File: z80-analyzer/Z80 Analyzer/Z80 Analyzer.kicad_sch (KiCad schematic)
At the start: 48 parts, among them J1 Conn_01x40_Pin, M1 TestPoint, U1 Z80CPU

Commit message: [Z80] Layout update
Mostly done, missing:
* Size
* Aligned slots for socket stack securing
* Grounding lead pads
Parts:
- added RN9: R_Pack04_SIP_Split, Resistor_SMD:R_Array_Convex_4x0603, symbol Device:R_Pack04_Split
- RN1, RN3, RN4, RN5, RN7, RN8: symbol Device:R_Pack04_SIP_Split -> Device:R_Pack04_Split
- RN2, RN6: value R_Pack04_SIP_Split -> R_Pack04_Split; symbol Device:R_Pack04_SIP_Split -> Device:R_Pack04_Split
- renumbered TP_RESET1 to RESET1
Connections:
- net at J1.29 (Pin_29): now also RN3.5 (R4.2); no longer RN3.8 (R4.2)
- net at J1.8 (Pin_8): now also RN5.8 (R1.2); no longer RN5.2 (R1.2)
- net at RN7.6 (R3.2): now also J1.28 (Pin_28)
- net at J1.31 (Pin_31): now also RN4.8 (R1.2); no longer RN4.2 (R1.2)
- net at J1.17 (Pin_17): now also RN1.7 (R2.2); no longer RN1.4 (R2.2)
- net at J1.16 (Pin_16): now also RN6.8 (R1.2); no longer RN6.2 (R1.2)
- net at J1.21 (Pin_21): now also RN1.5 (R4.2); no longer RN1.8 (R4.2)
- net at J1.14 (Pin_14): now also RN5.5 (R4.2); no longer RN5.8 (R4.2)
- net at RN8.6 (R3.2): now also J1.36 (Pin_36)
- net at J1.15 (Pin_15): now also RN1.8 (R1.2); no longer RN1.2 (R1.2)
- net at J1.23 (Pin_23): now also RN3.8 (R1.2); no longer RN3.2 (R1.2)
- net at J1.37 (Pin_37): now also RN4.5 (R4.2); no longer RN4.8 (R4.2)
- net at J1.7 (Pin_7): now also RN2.8 (R1.2); no longer RN2.2 (R1.2)
- net at J1.9 (Pin_9): now also RN2.7 (R2.2); no longer RN2.4 (R2.2)
- net at J1.25 (Pin_25): now also RN3.7 (R2.2); no longer RN3.4 (R2.2)
- net at J1.18 (Pin_18): now also RN6.7 (R2.2); no longer RN6.4 (R2.2)
- net at J1.10 (Pin_10): now also RN5.7 (R2.2); no longer RN5.4 (R2.2)
- net at J1.13 (Pin_13): now also RN2.5 (R4.2); no longer RN2.8 (R4.2)
- net at J1.22 (Pin_22): now also RN6.5 (R4.2); no longer RN6.8 (R4.2)
- net at J1.24 (Pin_24): now also RN7.8 (R1.2)
- net at J1.26 (Pin_26): now also RN7.7 (R2.2)
- net at J1.3 (Pin_3): now also RN9.6 (R3.2)
- net at J1.30 (Pin_30): now also RN7.5 (R4.2)
- net at J1.32 (Pin_32): now also RN8.8 (R1.2)
- net at J1.33 (Pin_33): now also RN4.7 (R2.2); no longer RN4.4 (R2.2)
- net at J1.34 (Pin_34): now also RN8.7 (R2.2)
- net at J1.38 (Pin_38): now also RN8.5 (R4.2)
- net at J1.4 (Pin_4): now also RN9.5 (R4.2)
- net A0 renamed S_A0
- net A1 renamed S_A1
- net S_A1: now also RN2.2 (R2.1); no longer RN2.3 (R2.1)
- net A10 renamed S_A10
- net S_A10: now also RN3.3 (R3.1); no longer RN3.5 (R3.1)
- net A11 renamed S_A11
- net S_A11: now also RN3.4 (R4.1); no longer RN3.7 (R4.1)
- net A12 renamed S_A12
- net A13 renamed S_A13
- net S_A13: now also RN4.2 (R2.1); no longer RN4.3 (R2.1)
- net A14 renamed S_A14
- net S_A14: now also RN4.3 (R3.1); no longer RN4.5 (R3.1)
- net A15 renamed S_A15
- net S_A15: now also RN4.4 (R4.1); no longer RN4.7 (R4.1)
- net A2 renamed S_A2
- net S_A2: now also RN2.3 (R3.1); no longer RN2.5 (R3.1)
- net A3 renamed S_A3
- net S_A3: now also RN2.4 (R4.1); no longer RN2.7 (R4.1)
- net A4 renamed S_A4
- net A5 renamed S_A5
- net S_A5: now also RN1.2 (R2.1); no longer RN1.3 (R2.1)
- net A6 renamed S_A6
- net S_A6: now also RN1.3 (R3.1); no longer RN1.5 (R3.1)
- net A7 renamed S_A7
- net S_A7: now also RN1.4 (R4.1); no longer RN1.7 (R4.1)
- net A8 renamed S_A8
- net A9 renamed S_A9
- net S_A9: now also RN3.2 (R2.1); no longer RN3.3 (R2.1)
- net BUSACK renamed S_BUSACK
- net BUSRQ renamed S_BUSRQ
- net CLK renamed S_CLK
- net S_CLK: now also RN9.3 (R3.1), RN9.4 (R4.1); no longer RN8.1 (R1.1)
- net D0 renamed S_D0
- net D1 renamed S_D1
- net S_D1: now also RN5.2 (R2.1); no longer RN5.3 (R2.1)
- net D2 renamed S_D2
- net S_D2: now also RN5.3 (R3.1); no longer RN5.5 (R3.1)
- net D3 renamed S_D3
- net S_D3: now also RN5.4 (R4.1); no longer RN5.7 (R4.1)
- net D4 renamed S_D4
- net D5 renamed S_D5
- net S_D5: now also RN6.2 (R2.1); no longer RN6.3 (R2.1)
- net D6 renamed S_D6
- net S_D6: now also RN6.3 (R3.1); no longer RN6.5 (R3.1)
- net D7 renamed S_D7
- net S_D7: now also RN6.4 (R4.1); no longer RN6.7 (R4.1)
- net HALT renamed S_HALT
- net INT renamed S_INT
- net S_INT: now also RN8.3 (R3.1); no longer RN8.5 (R3.1)
- net IORQ renamed S_IORQ
- net S_IORQ: now also RN7.3 (R3.1); no longer RN7.5 (R3.1)
- net M1 renamed S_M1
- net S_M1: now also RN8.2 (R2.1); no longer RN8.3 (R2.1)
- net MREQ renamed S_MREQ
- net S_MREQ: now also RN7.4 (R4.1); no longer RN7.7 (R4.1)
- net NMI renamed S_NMI
- net S_NMI: now also RN8.4 (R4.1); no longer RN8.7 (R4.1)
- net RD renamed S_RD
- net S_RD: now also RN7.2 (R2.1); no longer RN7.3 (R2.1)
- net RESET renamed S_RESET
- net S_RESET: now also RN8.1 (R1.1)
- net RFSH renamed S_RFSH
- net WAIT renamed S_WAIT
- net WR renamed S_WR
- no-connect marks 0 -> 2
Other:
- note added: "The following signals are not on the Logic Analyzer connector: BUSRQ BUSAQ HALT WAIT RFSH CLK is used for triggering"
- note removed: "The following signals are not on the Logic Analyzer connector: BUSRQ BUSAQ HALT WAIT RFSH RESET"

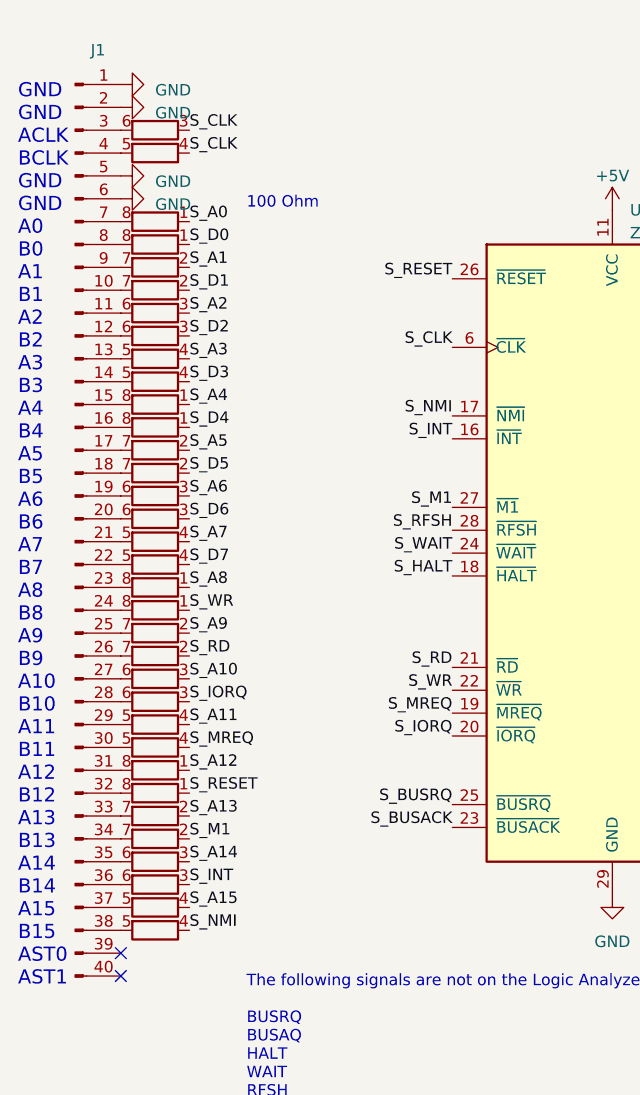
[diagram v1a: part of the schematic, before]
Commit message: [Z80] New routing, just needs rechecking now
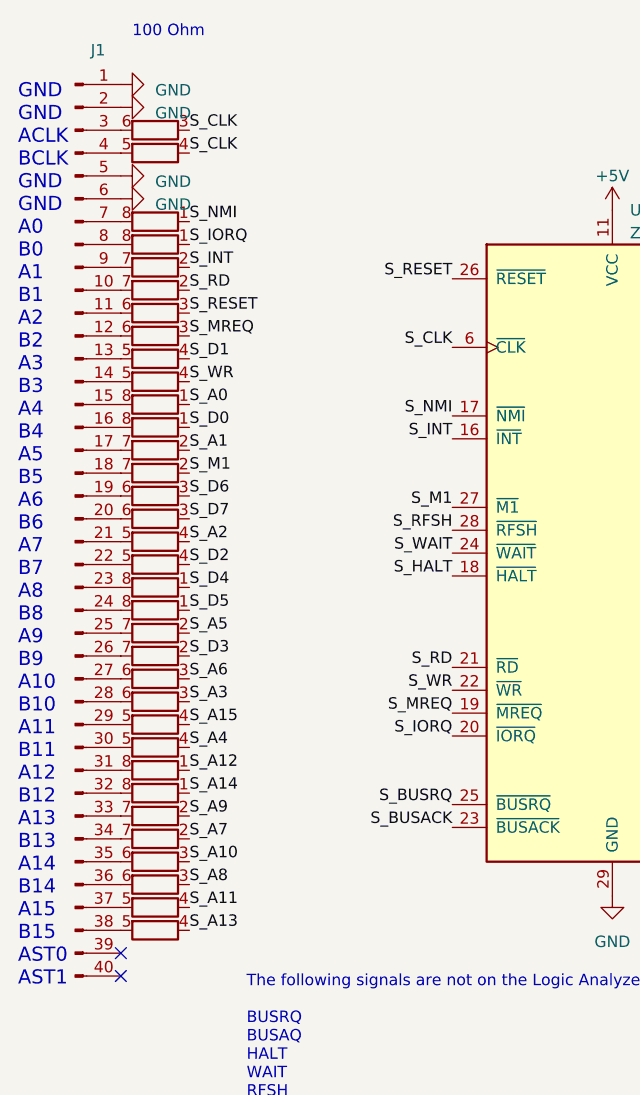
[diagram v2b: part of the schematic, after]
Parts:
- A0, A1, A10, A11, A12, A13, A14, A15, A2, A3, A4, A5, A6, A7, A8, A9, BUSACK1, BUSRQ1, CLK1, D0, D1, D2, D3, D4, D5, D6, D7, HALT1, INT1, IORQ1, M1, MREQ1, NMI1, RD1, RESET1, RFSH1, WAIT1, WR1: footprint TestPoint:TestPoint_Loop_D1.80mm_Drill1.0mm_Beaded -> CustomFootprints:TestPoint_Keystone_5021
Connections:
- net S_A0: now also RN1.1 (R1.1); no longer RN2.1 (R1.1)
- net S_A1: now also RN1.2 (R2.1); no longer RN2.2 (R2.1)
- net S_A10: now also RN4.3 (R3.1); no longer RN3.3 (R3.1)
- net S_A11: now also RN4.4 (R4.1); no longer RN3.4 (R4.1)
- net S_A13: now also RN8.4 (R4.1); no longer RN4.2 (R2.1)
- net S_A14: now also RN8.1 (R1.1); no longer RN4.3 (R3.1)
- net S_A15: now also RN3.4 (R4.1); no longer RN4.4 (R4.1)
- net S_A2: now also RN1.4 (R4.1); no longer RN2.3 (R3.1)
- net S_A3: now also RN7.3 (R3.1); no longer RN2.4 (R4.1)
- net S_A4: now also RN7.4 (R4.1); no longer RN1.1 (R1.1)
- net S_A5: now also RN3.2 (R2.1); no longer RN1.2 (R2.1)
- net S_A6: now also RN3.3 (R3.1); no longer RN1.3 (R3.1)
- net S_A7: now also RN8.2 (R2.1); no longer RN1.4 (R4.1)
- net S_A8: now also RN8.3 (R3.1); no longer RN3.1 (R1.1)
- net S_A9: now also RN4.2 (R2.1); no longer RN3.2 (R2.1)
- net S_D0: now also RN6.1 (R1.1); no longer RN5.1 (R1.1)
- net S_D1: now also RN2.4 (R4.1); no longer RN5.2 (R2.1)
- net S_D2: now also RN6.4 (R4.1); no longer RN5.3 (R3.1)
- net S_D3: now also RN7.2 (R2.1); no longer RN5.4 (R4.1)
- net S_D4: now also RN3.1 (R1.1); no longer RN6.1 (R1.1)
- net S_D5: now also RN7.1 (R1.1); no longer RN6.2 (R2.1)
- net S_D6: now also RN1.3 (R3.1); no longer RN6.3 (R3.1)
- net S_D7: now also RN6.3 (R3.1); no longer RN6.4 (R4.1)
- net S_INT: now also RN2.2 (R2.1); no longer RN8.3 (R3.1)
- net S_IORQ: now also RN5.1 (R1.1); no longer RN7.3 (R3.1)
- net S_M1: now also RN6.2 (R2.1); no longer RN8.2 (R2.1)
- net S_MREQ: now also RN5.3 (R3.1); no longer RN7.4 (R4.1)
- net S_NMI: now also RN2.1 (R1.1); no longer RN8.4 (R4.1)
- net S_RD: now also RN5.2 (R2.1); no longer RN7.2 (R2.1)
- net S_RESET: now also RN2.3 (R3.1); no longer RN8.1 (R1.1)
- net S_WR: now also RN5.4 (R4.1); no longer RN7.1 (R1.1)
